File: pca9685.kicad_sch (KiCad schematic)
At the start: 17 parts, among them J1 PCA9685 (2x) Pin Header, Q1 AOD417, Q2 AOD417, U1 SN74LVC1G04DBVR, U2 PCA9685PW, U3 PCA9685PW, Y1 SG-8002CA

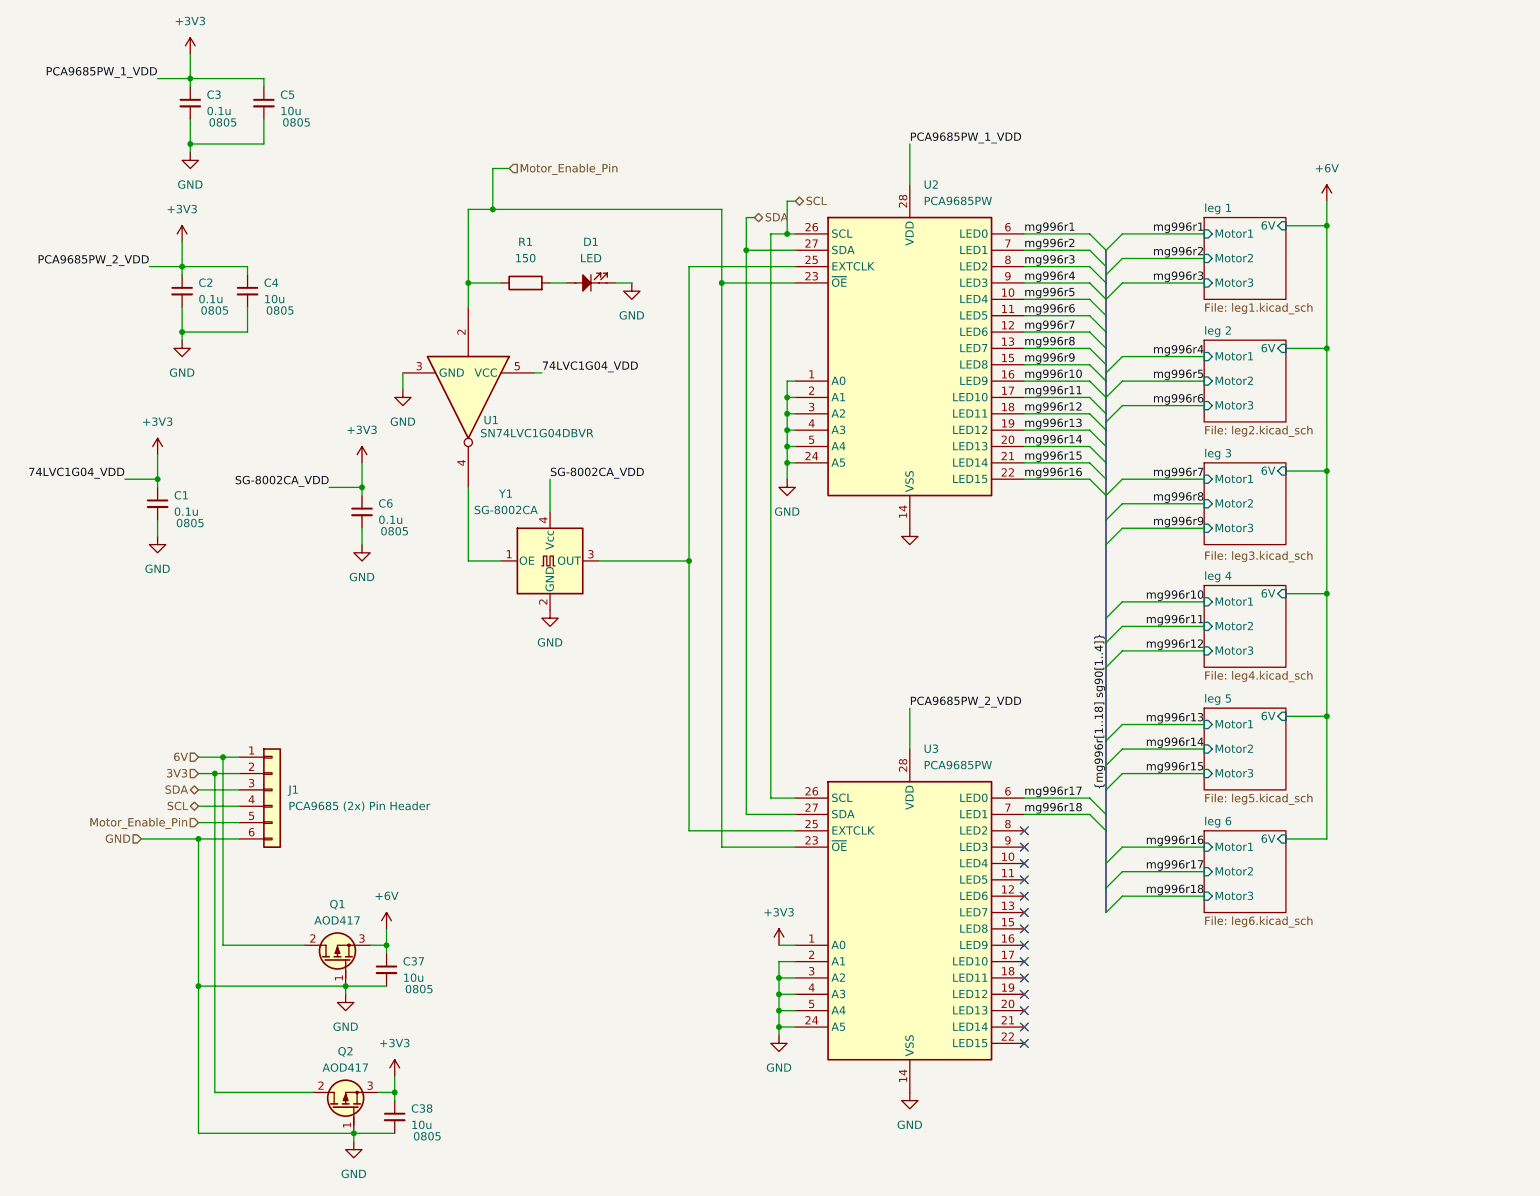
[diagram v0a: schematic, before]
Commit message: removed crystal, fixed caps
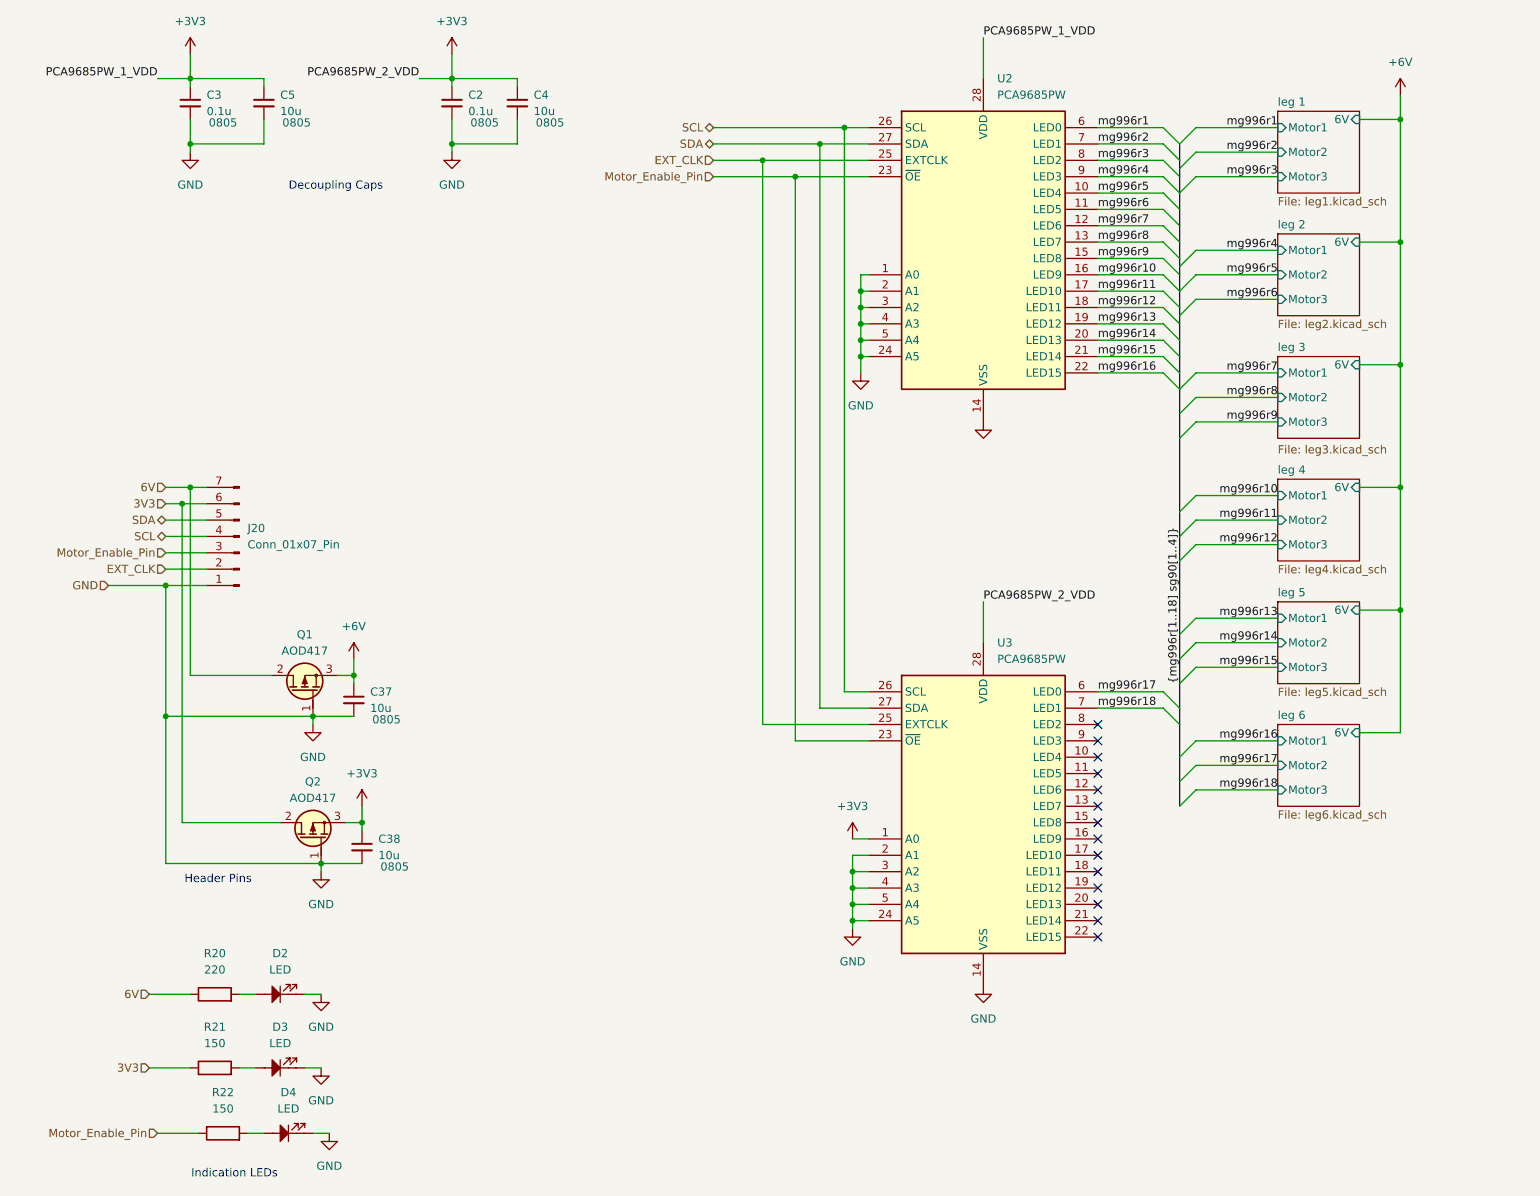
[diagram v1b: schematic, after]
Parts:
- removed C1, C6: 0.1u, Capacitor_SMD:C_0805_2012Metric_Pad1.18x1.45mm_HandSolder, symbol Device:C_Small
- removed D1: LED, LED_SMD:LED_PLCC-2_3.4x3.0mm_AK, symbol PCM_SL_Devices:LED
- removed J1: PCA9685 (2x) Pin Header, Connector_PinHeader_2.54mm:PinHeader_1x06_P2.54mm_Vertical, symbol PCM_4ms_Connector:Conn_01x06
- removed R1: 150K_0603, PCM_4ms_Resistor:R_0805_2012Metric, symbol PCM_4ms_Resistor:150K_0603
- removed U1: SN74LVC1G04DBVR, PCM_Package_TO_SOT_SMD_AKL:SOT-23-5_BigPads, symbol 74xGxx:74LVC1G04
- removed Y1: SG-8002CA, Oscillator:Oscillator_SMD_SeikoEpson_SG8002CA-4Pin_7.0x5.0mm, symbol Oscillator:SG-8002CA
- added D2, D3, D4: LED, LED_SMD:LED_PLCC-2_3.4x3.0mm_AK, symbol PCM_SL_Devices:LED
- added J20: Conn_01x07_Pin, Connector_PinHeader_2.54mm:PinHeader_1x07_P2.54mm_Vertical, symbol Connector:Conn_01x07_Pin
- added R20, R21, R22: 150K_0603, PCM_4ms_Resistor:R_0805_2012Metric, symbol PCM_4ms_Resistor:150K_0603
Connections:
- net 3V3: now also J20.6 (Pin_6), R21.1
- net 6V: now also J20.7 (Pin_7), R20.1
- net GND: now also D2.1, D3.1, D4.1, J20.1 (Pin_1)
- net Motor_Enable_Pin: now also J20.3 (Pin_3), R22.1
- net SCL: now also J20.4 (Pin_4)
- net SDA: now also J20.5 (Pin_5)
- net EXT_CLK: now reaches U2.25 (EXTCLK), U3.25 (EXTCLK)
- net EXT_CLK: now also J20.2 (Pin_2)
- new net: D3.2, R21.2
- new net: D4.2, R22.2
- new net: D2.2, R20.2
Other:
- note added: "Decoupling Caps"
- note added: "Header Pins"
- note added: "Indication LEDs"
- moved on the sheet: C2, C37, C38, C4, Q1, Q2, U2, U3

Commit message: added 3v3 line
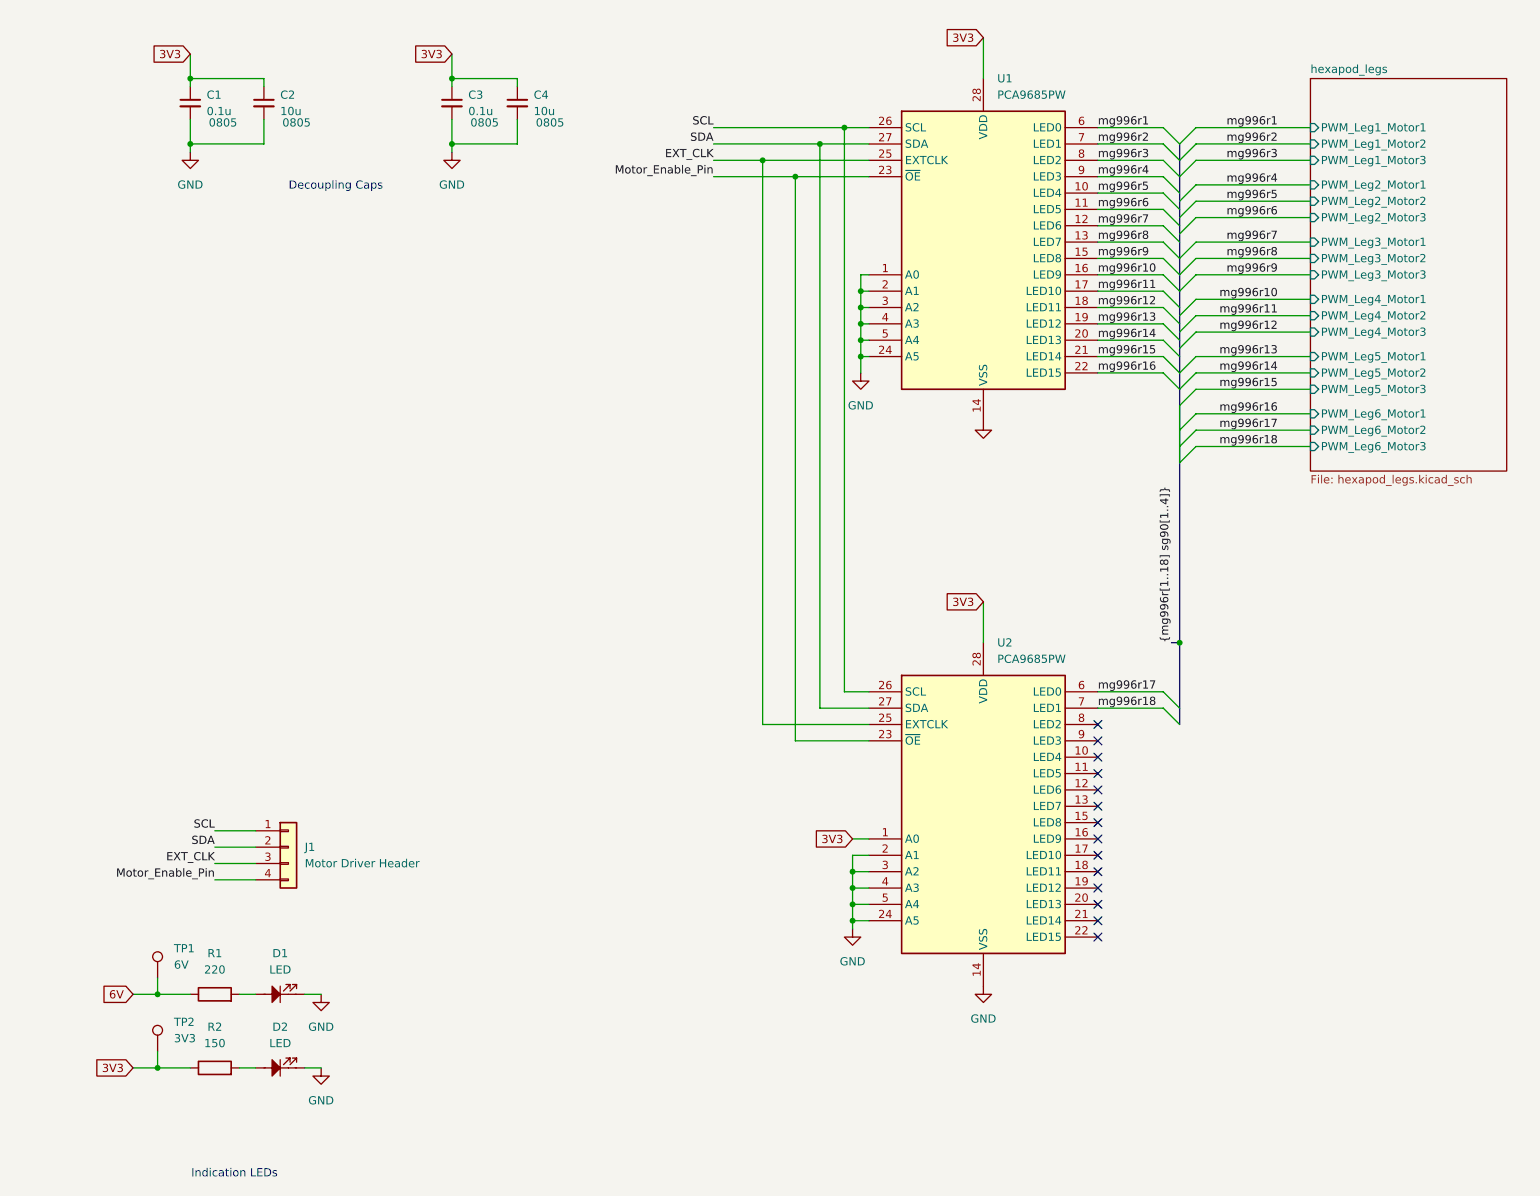
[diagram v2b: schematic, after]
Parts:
- removed C37, C38: 10u, Capacitor_SMD:C_0805_2012Metric_Pad1.18x1.45mm_HandSolder, symbol Device:C_Small
- removed D4: LED, LED_SMD:LED_PLCC-2_3.4x3.0mm_AK, symbol PCM_SL_Devices:LED
- removed J20: Conn_01x07_Pin, Connector_PinHeader_2.54mm:PinHeader_1x07_P2.54mm_Vertical, symbol Connector:Conn_01x07_Pin
- removed Q1, Q2: AOD417, PCM_Package_TO_SOT_SMD_AKL:TO-252-2, symbol PCM_Transistor_MOSFET_AKL:AOD417
- removed R22: 150K_0603, PCM_4ms_Resistor:R_0805_2012Metric, symbol PCM_4ms_Resistor:150K_0603
- added J1: Motor Driver Header, Connector_PinHeader_2.54mm:PinHeader_1x04_P2.54mm_Vertical, symbol PCM_4ms_Connector:Conn_01x04
- added TP1: 6V, symbol Connector:TestPoint
- added TP2: 3V3, symbol Connector:TestPoint
- D1: renamed from D2; footprint LED_SMD:LED_PLCC-2_3.4x3.0mm_AK -> PCM_4ms_LED:LED_0603_1608Metric
- D2: renamed from D3; footprint LED_SMD:LED_PLCC-2_3.4x3.0mm_AK -> PCM_4ms_LED:LED_0603_1608Metric
- renumbered C3 to C1, C5 to C2, C2 to C3, R20 to R1, R21 to R2, U2 to U1, U3 to U2
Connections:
- net +3V3 is gone; now on net 3V3: C1.1, C2.1, C3.1, C4.1, U1.28 (VDD), U2.1 (A0), U2.28 (VDD)
- net 3V3: now also TP2.1
- net 6V: now also TP1.1
- net EXT_CLK: now also J1.3 (Pin_3)
- net Motor_Enable_Pin: now also J1.4 (Pin_4)
- net SCL: now also J1.1 (Pin_1)
- net SDA: now also J1.2 (Pin_2)
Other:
- removed sheet leg 1
- removed sheet leg 2
- removed sheet leg 3
- removed sheet leg 4
- removed sheet leg 5
- removed sheet leg 6
- added sheet hexapod_legs (hexapod_legs.kicad_sch)
- note removed: "Header Pins"

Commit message: 20V line V2
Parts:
- renumbered J1 to J3
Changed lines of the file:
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@@
 		(dnp no)
 		(fields_autoplaced yes)
-		(property "Reference" "J1"
+		(property "Reference" "J3"
 			(at 57.15 144.7799 0)
 			(effects
@@
 			(project "Project-Star"
 				(path "/dfa3d008-01ec-4328-886a-a4a57a49a859/50ec6b1a-f906-43ba-9be1-78681b5bb3a1"
-					(reference "J1")
+					(reference "J3")
 					(unit 1)
 				)
